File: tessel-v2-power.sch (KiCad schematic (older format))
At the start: 54 parts, among them J301 CONN_01X02, Q301 MMSS8550, U301 MT9700, U302 MT9700, U305 AP3418

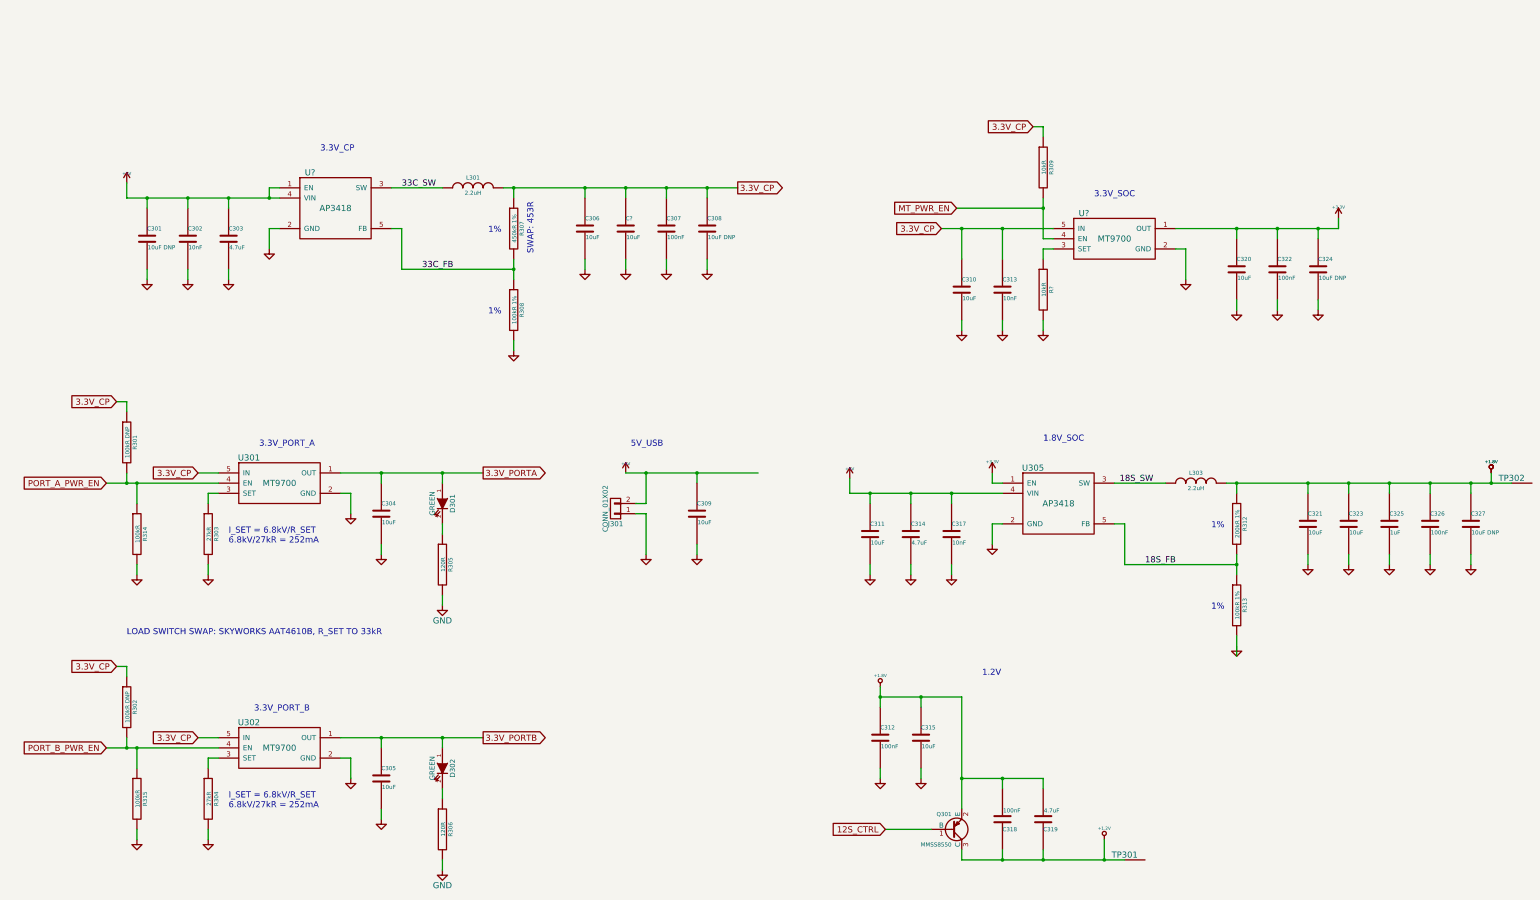
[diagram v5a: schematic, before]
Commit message: power mux is not done...oof.
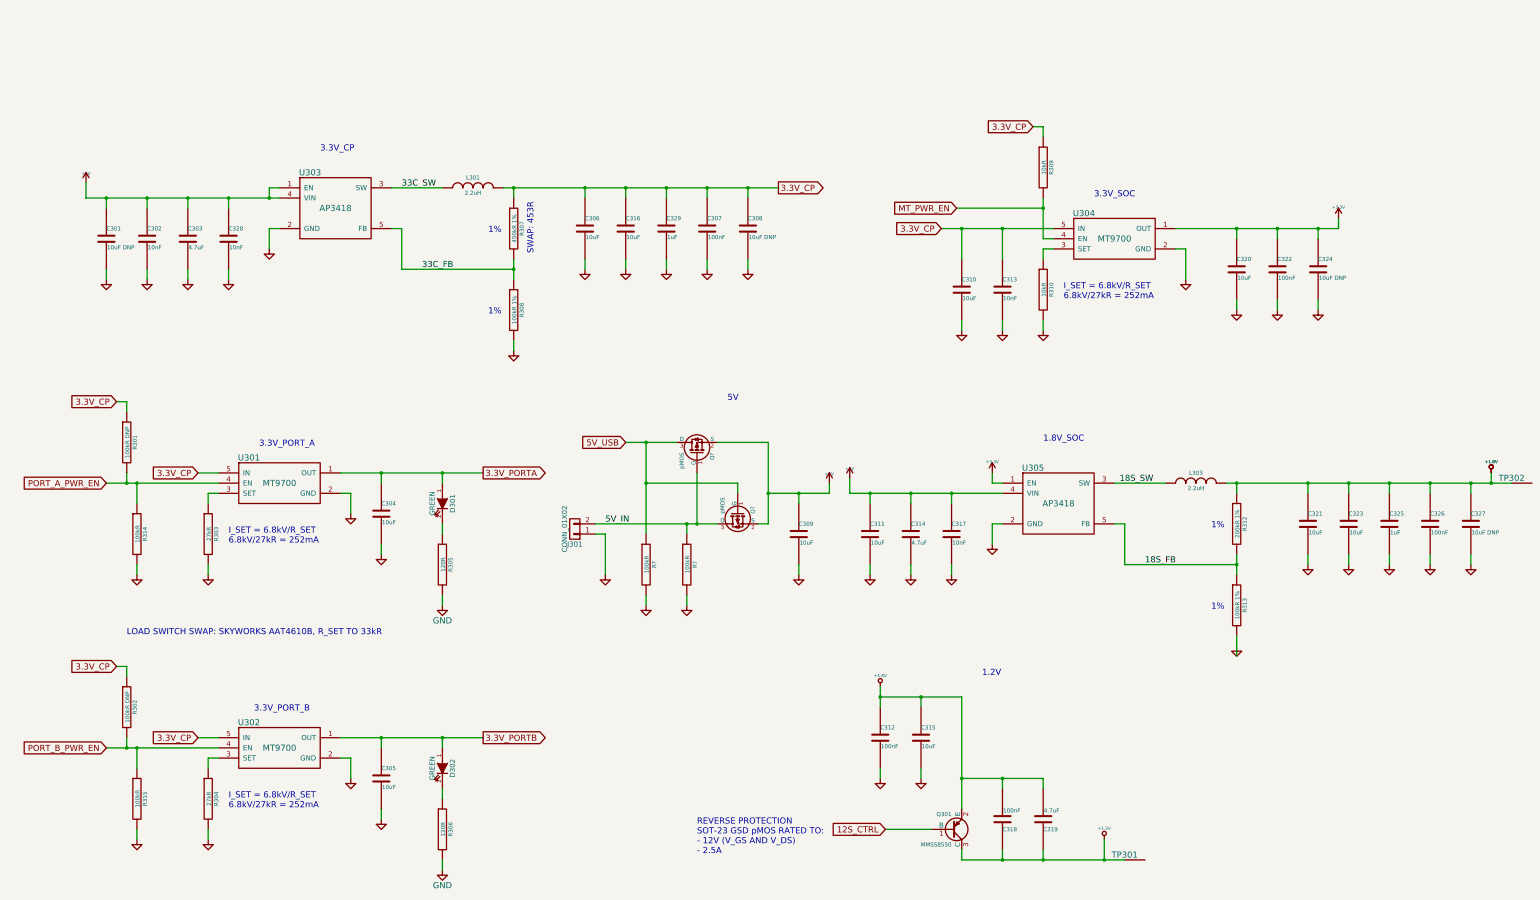
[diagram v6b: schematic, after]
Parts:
- added C328: 10nF, tm-kicad-lib:SMD-0402-C, symbol TM_C
- added C329: 1uF, tm-kicad-lib:SMD-0402-C, symbol TM_C
- added Q? (x2): pMOS, Housings_SOT-23_SOT-143_TSOT-6:SOT-23, symbol pMOS
- added R? (x2): 100kR, tm-kicad-lib:SMD-0402-R, symbol TM_R
- gave numbers to parts that had none: 4
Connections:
- net +5V: now also C328.1, Q?.2 (S), Q?.2 (S); no longer J301.2 (P2)
- net 3.3V_CP: now also C329.1
- net GND: now also C328.2, C329.2, R?.2, R?.2
- new net 5V_IN: J301.2 (P2), Q?.1 (G), Q?.3 (D), R?.1
- new net 5V_USB: Q?.1 (G), Q?.3 (D), R?.1
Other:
- note added: "5V"
- note added: "REVERSE PROTECTION\nSOT-23 GSD pMOS RATED TO:\n- 12V (V_GS AND V_DS)\n- 2.5A"
- note removed: "5V_USB"
- moved on the sheet: C301, C302, C303, C307, C308, C309, J301

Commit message: reverse protection with backfeed done, power plant rewoked. time to to the layout.
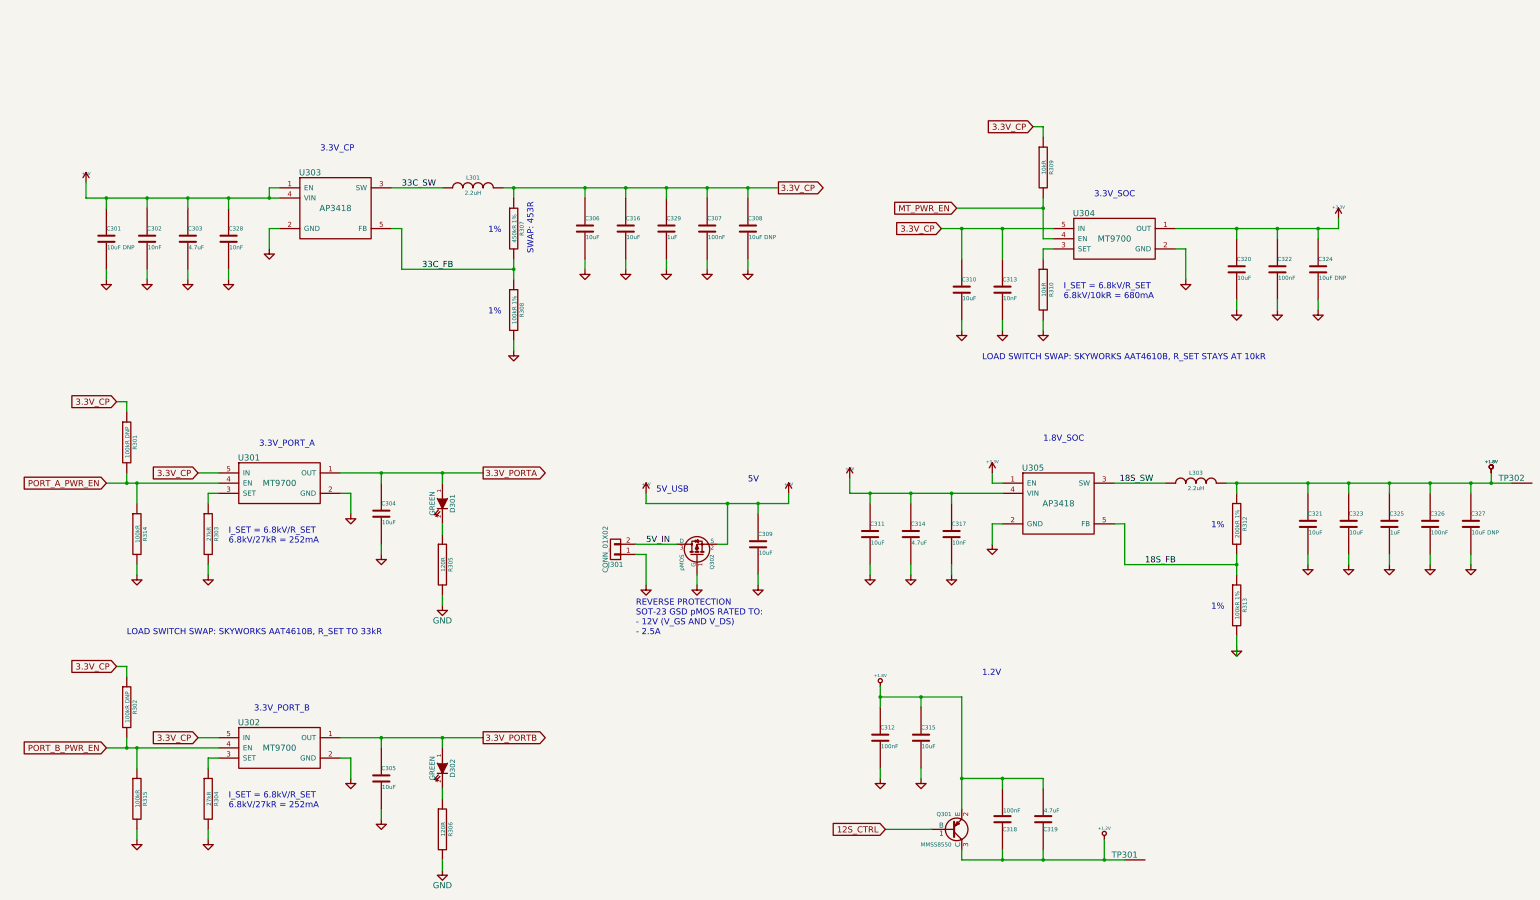
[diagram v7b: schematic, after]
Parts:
- removed Q?: pMOS, Housings_SOT-23_SOT-143_TSOT-6:SOT-23, symbol pMOS
- removed R? (x2): 100kR, tm-kicad-lib:SMD-0402-R, symbol TM_R
- gave numbers to parts that had none: 1
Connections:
- net 5V_USB is gone; now on net GND: Q302.1 (G)
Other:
- note added: "5V_USB"
- note added: "I_SET = 6.8kV/R_SET\n6.8kV/10kR = 680mA"
- note added: "LOAD SWITCH SWAP: SKYWORKS AAT4610B, R_SET STAYS AT 10kR"
- moved on the sheet: C309, J301, Q302

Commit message: bigger SAM
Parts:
- U301, U302, U304: footprint (none) -> Housings_SOT-23_SOT-143_TSOT-6:SOT-23-5
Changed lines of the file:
@@
 F 0 "U301" H 3100 5950 60  0000 C CNN
 F 1 "MT9700" H 3400 5700 60  0000 C CNN
-F 2 "" H 3400 5700 60  0000 C CNN
+F 2 "Housings_SOT-23_SOT-143_TSOT-6:SOT-23-5" H 3400 5700 60  0001 C CNN
 F 3 "" H 3400 5700 60  0000 C CNN
 	1    3400 5700
@@
 F 0 "U302" H 3100 8550 60  0000 C CNN
 F 1 "MT9700" H 3400 8300 60  0000 C CNN
-F 2 "" H 3400 8300 60  0000 C CNN
+F 2 "Housings_SOT-23_SOT-143_TSOT-6:SOT-23-5" H 3400 8300 60  0001 C CNN
 F 3 "" H 3400 8300 60  0000 C CNN
 	1    3400 8300
@@
 F 0 "U304" H 11300 3550 60  0000 C CNN
 F 1 "MT9700" H 11600 3300 60  0000 C CNN
-F 2 "" H 11600 3300 60  0000 C CNN
+F 2 "Housings_SOT-23_SOT-143_TSOT-6:SOT-23-5" H 11600 3300 60  0001 C CNN
 F 3 "" H 11600 3300 60  0000 C CNN
 	1    11600 3300
